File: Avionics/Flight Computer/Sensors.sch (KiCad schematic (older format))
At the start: 0 parts

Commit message: Lots of power tree and layout work
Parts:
- added U5: MPU-9250, Housings_DFN_QFN:QFN-24-1EP_3x3mm_Pitch0.4mm, symbol MPU-9250
- added U6: Si7006-A20-IM1, Housings_DFN_QFN:DFN-6-1EP_3x3mm_Pitch0.95mm, symbol Si7006-A20-IM1
- added U7: LPS25HB, Housings_LGA:HLGA-10L_2.5x2.5mm_Pitch0.6mm, symbol LPS25HB
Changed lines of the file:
@@
 LIBS:graphic
 LIBS:power
+LIBS:interface
+LIBS:linear
+LIBS:74xgxx
+LIBS:74xx
+LIBS:ac-dc
+LIBS:actel
+LIBS:adc-dac
+LIBS:allegro
+LIBS:Altera
+LIBS:analog_devices
+LIBS:analog_switches
+LIBS:Power_Management
+LIBS:powerint
 LIBS:Flight Computer-cache
-EELAYER 25 0
+EELAYER 26 0
 EELAYER END
 $Descr A4 11693 8268
 encoding utf-8
-Sheet 1 7
+Sheet 7 7
 Title ""
 Date ""
@@
 Comment4 ""
 $EndDescr
+$Comp
+L Si7006-A20-IM1 U6
+U 1 1 58B10937
+P 5800 3600
+F 0 "U6" H 5950 3850 50  0000 C CNN
+F 1 "Si7006-A20-IM1" H 6050 3350 50  0000 C CNN
+F 2 "Housings_DFN_QFN:DFN-6-1EP_3x3mm_Pitch0.95mm" H 5800 3200 50  0001 C CNN
+F 3 "http://www.silabs.com/documents/public/data-sheets/Si7006-A20.pdf" H 5800 4000 50  0001 C CNN
+	1    5800 3600
+	1    0    0    -1
+$EndComp
+$Comp
+L LPS25HB U7
+U 1 1 58AB52C0
+P 5850 1900
+F 0 "U7" H 5520 1946 50  0000 R CNN
+F 1 "LPS25HB" H 5520 1855 50  0000 R CNN
+F 2 "Housings_LGA:HLGA-10L_2.5x2.5mm_Pitch0.6mm" H -250 1150 50  0001 C CIN
+F 3 "http://www.st.com/resource/en/datasheet/lps25hb.pdf" H -250 1250 50  0001 C CNN
+	1    5850 1900
+	1    0    0    -1
+$EndComp
+$Comp
+L MPU-9250 U5
+U 1 1 58AB562F
+P 3400 2850
+F 0 "U5" H 3400 1864 50  0000 C CNN
+F 1 "MPU-9250" H 3400 1773 50  0000 C CNN
+F 2 "Housings_DFN_QFN:QFN-24-1EP_3x3mm_Pitch0.4mm" H 200 -1400 50  0001 C CNN
+F 3 "https://www.invensense.com/wp-content/uploads/2015/02/PS-MPU-9250A-01-v1.1.pdf" H 200 900 50  0001 C CNN
+	1    3400 2850
+	1    0    0    -1
+$EndComp
 $EndSCHEMATC

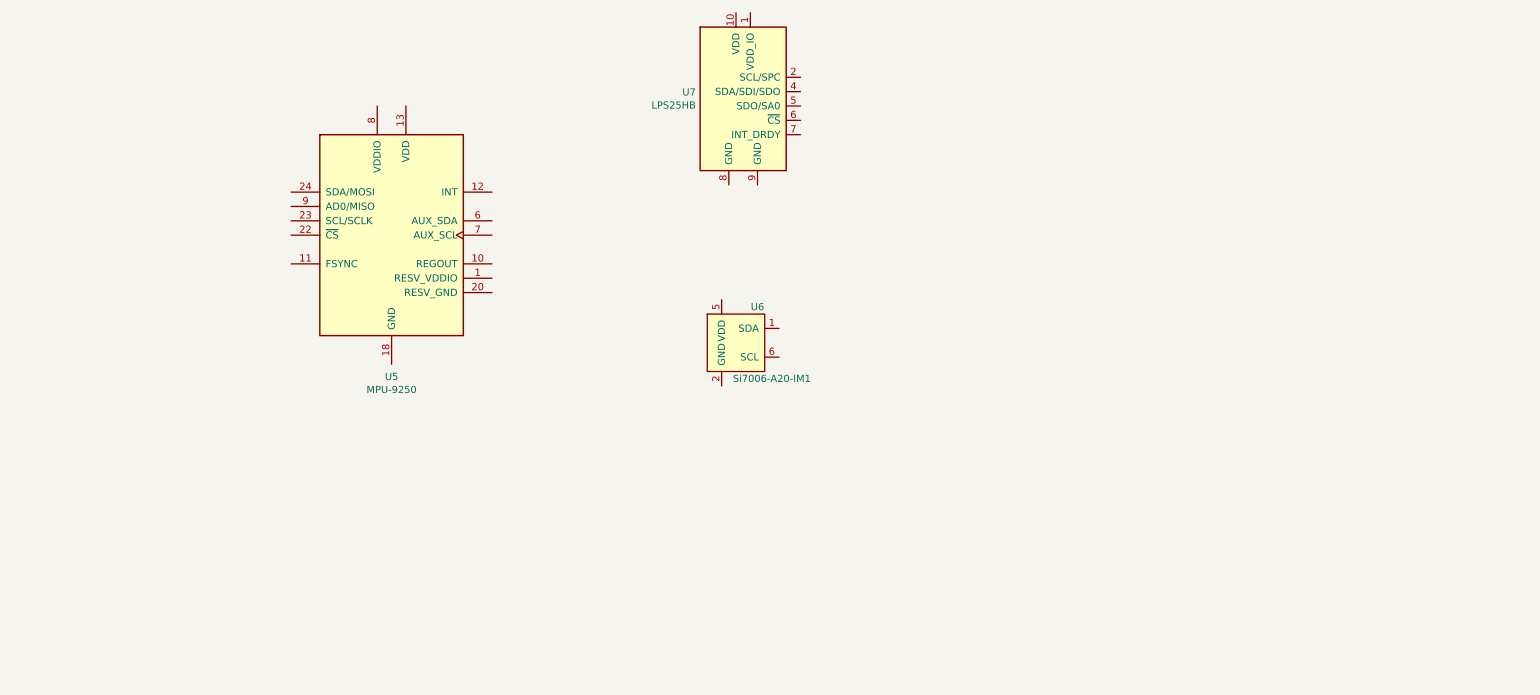
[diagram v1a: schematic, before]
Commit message: Restarted initial layout and cleaned up decoupling/RF layout.
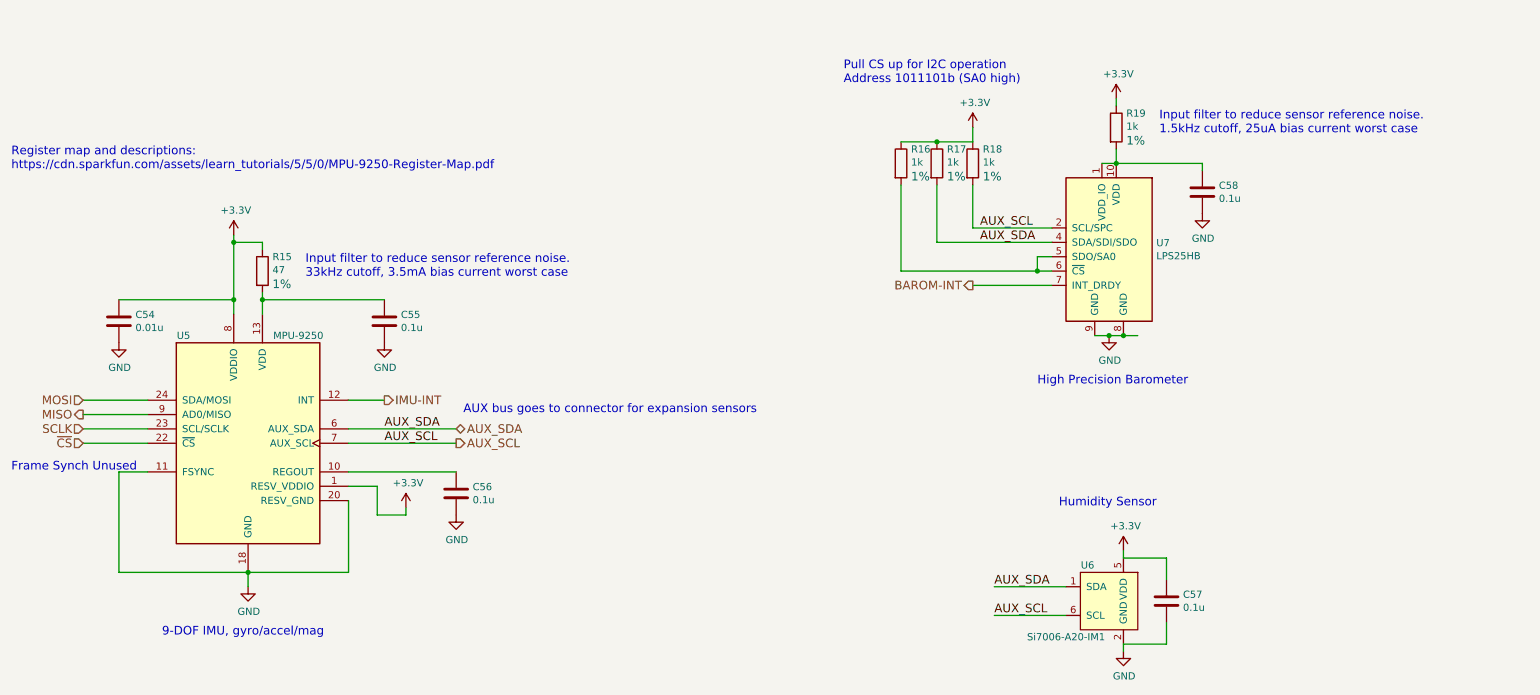
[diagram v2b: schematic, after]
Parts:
- added C54: 0.01u, Capacitors_SMD:C_0402, symbol C
- added C55, C56, C57, C58: 0.1u, Capacitors_SMD:C_0402, symbol C
- added R15: 47, Resistors_SMD:R_0402, symbol R
- added R16, R17, R18, R19: 1k, Resistors_SMD:R_0402, symbol R
- U5: footprint Housings_DFN_QFN:QFN-24-1EP_3x3mm_Pitch0.4mm -> Housings_DFN_QFN:QFN-24-1EP_3x3mm_Pitch0.4mm_MPU-9250
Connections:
- net at U7.1 (VDD_IO): now also U7.10 (VDD), C58.1, R19.2
- net AUX_SCL: now reaches U7.2 (SCL/SPC)
- net AUX_SCL: now also U5.7 (AUX_SCL), U6.6 (SCL), R18.2
- net GND: now reaches U7.3 (Reserved)
- net GND: now also U5.11 (FSYNC), U5.18 (GND), U5.20 (RESV_GND), U6.2 (GND), U7.8 (GND), U7.9 (GND), C54.2, C55.2, C56.2, C57.2, C58.2
- net AUX_SDA: now reaches U7.4 (SDA/SDI/SDO)
- net AUX_SDA: now also U5.6 (AUX_SDA), U6.1 (SDA), R17.2
- net at U7.5 (SDO/SA0): now also U7.6 (~CS), R16.2
- net BAROM-INT: now reaches U7.7 (INT_DRDY)
- net +3V3: now reaches U5.1 (RESV_VDDIO)
- net +3V3: now also U5.8 (VDDIO), U6.5 (VDD), C54.1, C57.1, R15.1, R16.1, R17.1, R18.1, R19.1
- net at U5.10 (REGOUT): now also C56.1
- net IMU-INT: now reaches U5.12 (INT)
- net at U5.13 (VDD): now also C55.1, R15.2
- net ~CS: now reaches U5.22 (~CS)
- net SCLK: now reaches U5.23 (SCL/SCLK)
- net MOSI: now reaches U5.24 (SDA/MOSI)
- net MISO: now reaches U5.9 (AD0/MISO)
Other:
- note added: "9-DOF IMU, gyro/accel/mag"
- note added: "AUX bus goes to connector for expansion sensors"
- note added: "Frame Synch Unused"
- note added: "High Precision Barometer"
- note added: "Humidity Sensor"
- note added: "Input filter to reduce sensor reference noise. \n1.5kHz cutoff, 25uA bias current worst case"
- note added: "Input filter to reduce sensor reference noise. \n33kHz cutoff, 3.5mA bias current worst case"
- note added: "Pull CS up for I2C operation\nAddress 1011101b (SA0 high)"
- note added: "Register map and descriptions: \nhttps://cdn.sparkfun.com/assets/learn_tutorials/5/5/0/MPU-9250-Register-Map.pdf"
- moved on the sheet: U5, U6

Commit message: Nearly completed initial placement.
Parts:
- removed C57: 0.1u, Capacitors_SMD:C_0402, symbol C
- removed U6: Si7006-A20-IM1, Housings_DFN_QFN:DFN-6-1EP_3x3mm_Pitch0.95mm, symbol Si7006-A20-IM1
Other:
- note added: "Frame Sync Unused"
- note added: "Layout Note: Exposed pad is NC. Do not solder the exposed pad."
- note removed: "Frame Synch Unused"
- note removed: "Humidity Sensor"
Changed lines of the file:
@@
 $EndDescr
-$Comp
-L Si7006-A20-IM1 U6
-U 1 1 58B10937
-P 8400 5400
-F 0 "U6" H 8550 5650 50  0000 C CNN
-F 1 "Si7006-A20-IM1" H 8700 5150 50  0000 C CNN
-F 2 "Housings_DFN_QFN:DFN-6-1EP_3x3mm_Pitch0.95mm" H 8400 5000 50  0001 C CNN
-F 3 "http://www.silabs.com/documents/public/data-sheets/Si7006-A20.pdf" H 8400 5800 50  0001 C CNN
-	1    8400 5400
-	-1   0    0    -1
-$EndComp
 $Comp
 L MPU-9250 U5
@@
 $EndComp
 $Comp
-L GND #PWR071
+L GND #PWR097
 U 1 1 58B4AF5E
 P 2400 5300
-F 0 "#PWR071" H -1950 1500 50  0001 C CNN
+F 0 "#PWR097" H -1950 1500 50  0001 C CNN
 F 1 "GND" H 2405 5127 50  0000 C CNN
 F 2 "" H -1950 1750 50  0001 C CNN
@@
 $EndComp
 $Comp
-L +3.3V #PWR072
+L +3.3V #PWR098
 U 1 1 58B4AFA2
 P 2300 2850
-F 0 "#PWR072" H -2200 -700 50  0001 C CNN
+F 0 "#PWR098" H -2200 -700 50  0001 C CNN
 F 1 "+3.3V" H 2315 3023 50  0000 C CNN
 F 2 "" H -2200 -550 50  0001 C CNN
@@
 $EndComp
 $Comp
-L GND #PWR073
+L GND #PWR099
 U 1 1 58B4B105
 P 8400 3550
-F 0 "#PWR073" H 4050 -250 50  0001 C CNN
+F 0 "#PWR099" H 4050 -250 50  0001 C CNN
 F 1 "GND" H 8405 3377 50  0000 C CNN
 F 2 "" H 4050 0   50  0001 C CNN
@@
 Connection ~ 8400 3550
 $Comp
-L GND #PWR074
-U 1 1 58B4B122
-P 8500 5750
-F 0 "#PWR074" H 4150 1950 50  0001 C CNN
-F 1 "GND" H 8505 5577 50  0000 C CNN
-F 2 "" H 4150 2200 50  0001 C CNN
-F 3 "" H 4150 2200 50  0001 C CNN
-	1    8500 5750
-	1    0    0    -1
-$EndComp
-$Comp
-L +3.3V #PWR075
+L +3.3V #PWR0100
 U 1 1 58B4B14B
 P 8450 1900
-F 0 "#PWR075" H 3950 -1650 50  0001 C CNN
+F 0 "#PWR0100" H 3950 -1650 50  0001 C CNN
 F 1 "+3.3V" H 8465 2073 50  0000 C CNN
 F 2 "" H 3950 -1500 50  0001 C CNN
@@
 Wire Wire Line
 	8350 2350 9050 2350
-$Comp
-L +3.3V #PWR076
-U 1 1 58B4B1B7
-P 8500 5050
-F 0 "#PWR076" H 4000 1500 50  0001 C CNN
-F 1 "+3.3V" H 8515 5223 50  0000 C CNN
-F 2 "" H 4000 1650 50  0001 C CNN
-F 3 "" H 4000 1650 50  0001 C CNN
-	1    8500 5050
-	1    0    0    -1
-$EndComp
-$Comp
-L C C57
-U 1 1 58B4B2E1
-P 8800 5400
-F 0 "C57" H 8915 5446 50  0000 L CNN
-F 1 "0.1u" H 8915 5355 50  0000 L CNN
-F 2 "Capacitors_SMD:C_0402" H 2038 1500 50  0001 C CNN
-F 3 "" H 2000 1650 50  0001 C CNN
-F 4 "50V" H 2100 1600 60  0001 L CNN "Voltage"
-F 5 "20%" H 2100 1700 60  0001 L CNN "Tolerance"
-F 6 "X7R" H 2050 1800 60  0001 L CNN "Type"
-F 7 "0402" H 2050 1500 60  0001 L CNN "Package"
-	1    8800 5400
-	1    0    0    -1
-$EndComp
-Wire Wire Line
-	8500 5700 8800 5700
-Wire Wire Line
-	8800 5700 8800 5550
-Wire Wire Line
-	8800 5250 8800 5100
-Wire Wire Line
-	8800 5100 8500 5100
-Wire Wire Line
-	8500 5100 8500 5050
-Wire Wire Line
-	8500 5750 8500 5700
-Wire Wire Line
-	8100 5500 7600 5500
-Wire Wire Line
-	7600 5300 8100 5300
-Text Label 7600 5500 0    60   ~ 0
-AUX_SCL
-Text Label 7600 5300 0    60   ~ 0
-AUX_SDA
 Wire Wire Line
 	7450 2800 8000 2800
@@
 Connection ~ 8450 2350
 $Comp
-L GND #PWR077
+L GND #PWR0101
 U 1 1 58B4B9E9
 P 9050 2700
-F 0 "#PWR077" H 4700 -1100 50  0001 C CNN
+F 0 "#PWR0101" H 4700 -1100 50  0001 C CNN
 F 1 "GND" H 9055 2527 50  0000 C CNN
 F 2 "" H 4700 -850 50  0001 C CNN
@@
 Connection ~ 8500 3550
 $Comp
-L +3.3V #PWR078
+L +3.3V #PWR0102
 U 1 1 58B4C158
 P 7450 2100
-F 0 "#PWR078" H 2950 -1450 50  0001 C CNN
+F 0 "#PWR0102" H 2950 -1450 50  0001 C CNN
 F 1 "+3.3V" H 7465 2273 50  0000 C CNN
 F 2 "" H 2950 -1300 50  0001 C CNN
@@
 Text Notes 7900 3900 0    60   ~ 0
 High Precision Barometer
-Text Notes 8050 4750 0    60   ~ 0
-Humidity Sensor
 Text Notes 1800 5650 0    60   ~ 0
 9-DOF IMU, gyro/accel/mag
@@
 	3100 4500 3850 4500
 $Comp
-L GND #PWR079
+L GND #PWR0103
 U 1 1 58B4FB3E
 P 3850 4800
-F 0 "#PWR079" H -500 1000 50  0001 C CNN
+F 0 "#PWR0103" H -500 1000 50  0001 C CNN
 F 1 "GND" H 3855 4627 50  0000 C CNN
 F 2 "" H -500 1250 50  0001 C CNN
@@
 	3500 4800 3500 4750
 $Comp
-L +3.3V #PWR080
+L +3.3V #PWR0104
 U 1 1 58B50137
 P 3500 4750
-F 0 "#PWR080" H -1000 1200 50  0001 C CNN
+F 0 "#PWR0104" H -1000 1200 50  0001 C CNN
 F 1 "+3.3V" H 3515 4923 50  0000 C CNN
 F 2 "" H -1000 1350 50  0001 C CNN
@@
 IMU-INT
 $Comp
-L GND #PWR081
+L GND #PWR0105
 U 1 1 58B505FC
 P 3350 3600
-F 0 "#PWR081" H -1000 -200 50  0001 C CNN
+F 0 "#PWR0105" H -1000 -200 50  0001 C CNN
 F 1 "GND" H 3355 3427 50  0000 C CNN
 F 2 "" H -1000 50  50  0001 C CNN
@@
 Input filter to reduce sensor reference noise. \n33kHz cutoff, 3.5mA bias current worst case
 $Comp
-L GND #PWR082
+L GND #PWR0106
 U 1 1 58B50B96
 P 1500 3600
-F 0 "#PWR082" H -2850 -200 50  0001 C CNN
+F 0 "#PWR0106" H -2850 -200 50  0001 C CNN
 F 1 "GND" H 1505 3427 50  0000 C CNN
 F 2 "" H -2850 50  50  0001 C CNN
@@
 Connection ~ 2400 5200
 Text Notes 750  4500 0    60   ~ 0
-Frame Synch Unused
+Frame Sync Unused
 Text Notes 750  2400 0    60   ~ 0
 Register map and descriptions: \nhttps://cdn.sparkfun.com/assets/learn_tutorials/5/5/0/MPU-9250-Register-Map.pdf
@@
 $Comp
 L LPS25HB U7
-U 1 1 58B2400D
+U 1 1 58B3E15F
 P 8400 2950
+AR Path="/58B3E15F" Ref="U7"  Part="1"
+AR Path="/58AA09D0/58B3E15F" Ref="U7"  Part="1"
 F 0 "U7" H 8071 2996 50  0000 R CNN
 F 1 "LPS25HB" H 8071 2905 50  0000 R CNN
-F 2 "Housings_LGA:HLGA-10L_2.5x2.5mm_Pitch0.6mm" H -950 800 50  0001 C CIN
-F 3 "http://www.st.com/resource/en/datasheet/lps25hb.pdf" H -950 900 50  0001 C CNN
+F 2 "Housings_LGA:HLGA-10L_2.5x2.5mm_Pitch0.6mm" H -1250 700 50  0001 C CIN
+F 3 "http://www.st.com/resource/en/datasheet/lps25hb.pdf" H -1250 800 50  0001 C CNN
 	1    8400 2950
 	-1   0    0    -1
 $EndComp
+Text Notes 1000 5900 0    60   ~ 0
+Layout Note: Exposed pad is NC. Do not solder the exposed pad.
 $EndSCHEMATC

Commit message: Added additional pinout
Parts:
- U7: symbol LPS25HB -> LPS25HB-RESCUE-Flight_Computer
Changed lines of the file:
@@
 	1    0    0    -1
 $EndComp
-Wire Wire Line
-	8300 3550 8600 3550
 Connection ~ 8400 3550
 $Comp
@@
 Text Notes 8750 2150 0    60   ~ 0
 Input filter to reduce sensor reference noise. \n1.5kHz cutoff, 25uA bias current worst case
-Connection ~ 8500 3550
 $Comp
 L +3.3V #PWR0102
@@
 AUX bus goes to connector for expansion sensors
 $Comp
-L LPS25HB U7
+L LPS25HB-RESCUE-Flight_Computer U7
 U 1 1 58B3E15F
 P 8400 2950
@@
 Text Notes 1000 5900 0    60   ~ 0
 Layout Note: Exposed pad is NC. Do not solder the exposed pad.
+Wire Wire Line
+	8300 3550 8500 3550
 $EndSCHEMATC

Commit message: Wired up everything and started rearranging layout
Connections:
- net BAROM-INT: no longer names the net of U7.7 (INT_DRDY)
- no-connect marks 0 -> 1
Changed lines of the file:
@@
 $Descr A4 11693 8268
 encoding utf-8
-Sheet 7 9
+Sheet 7 8
 Title ""
 Date ""
@@
 Connection ~ 2300 3300
 Wire Wire Line
-	8000 3200 7450 3200
-Text HLabel 7450 3200 0    60   Output ~ 0
-BAROM-INT
-Wire Wire Line
 	1700 4500 1500 4500
 Wire Wire Line
@@
 Text HLabel 3850 4200 2    60   BiDi ~ 0
 AUX_SDA
-Text HLabel 3850 4300 2    60   Output ~ 0
+Text HLabel 3850 4300 2    60   BiDi ~ 0
 AUX_SCL
 Text Notes 3900 4100 0    60   ~ 0
@@
 Wire Wire Line
 	8300 3550 8500 3550
+NoConn ~ 8000 3200
 $EndSCHEMATC
